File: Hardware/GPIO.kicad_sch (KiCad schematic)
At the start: 8 parts, among them J2 GPIO Breakout

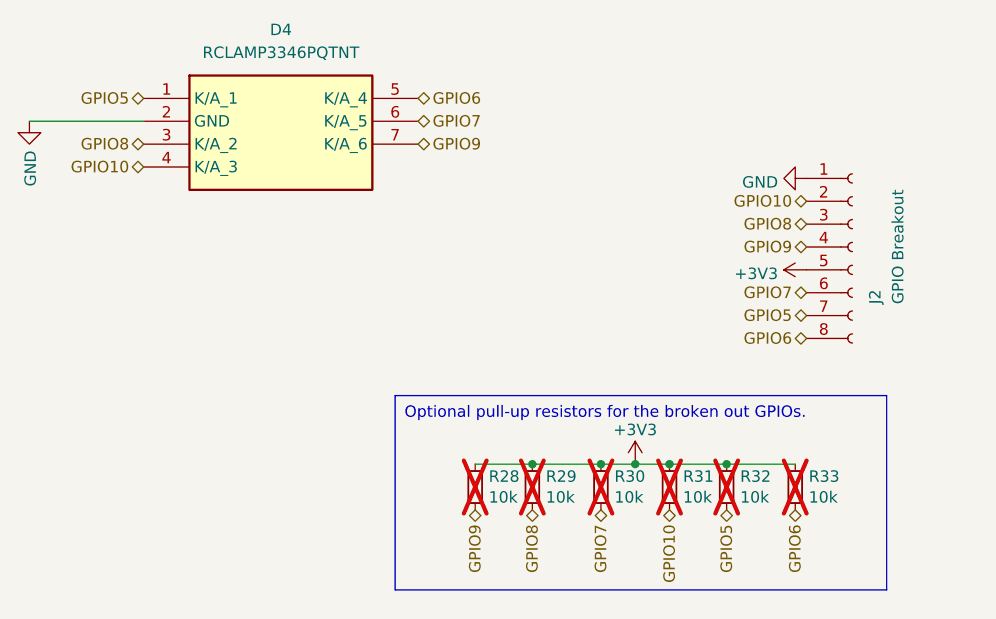
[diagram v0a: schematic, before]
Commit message: cleaned up schematic and bom
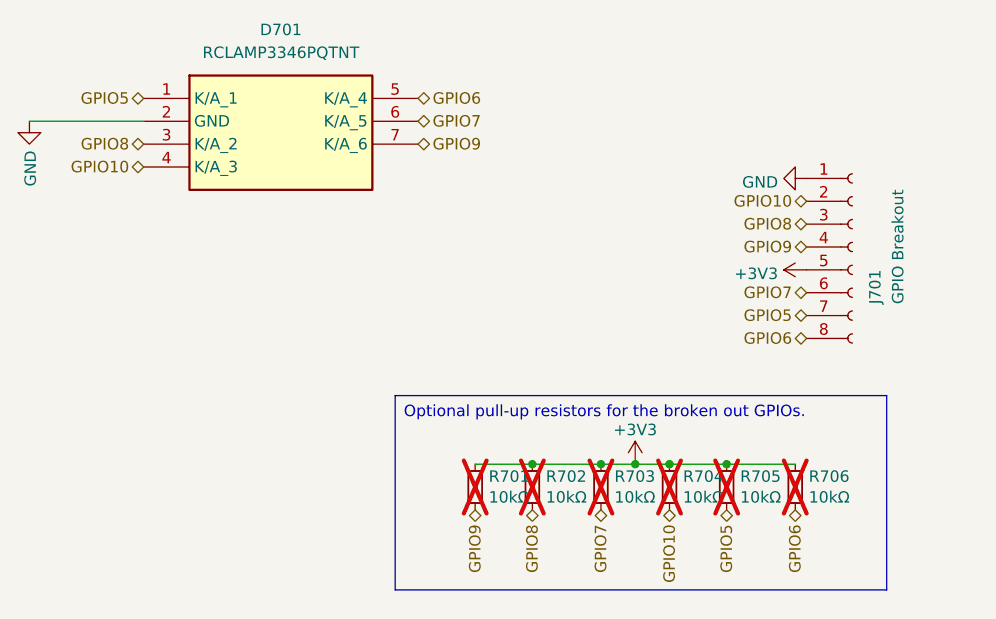
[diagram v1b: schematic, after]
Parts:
- R701: renamed from R28; value 10k -> 10kΩ
- R702: renamed from R29; value 10k -> 10kΩ
- R703: renamed from R30; value 10k -> 10kΩ
- R704: renamed from R31; value 10k -> 10kΩ
- R705: renamed from R32; value 10k -> 10kΩ
- R706: renamed from R33; value 10k -> 10kΩ
- renumbered D4 to D701, J2 to J701
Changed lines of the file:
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@@
 (kicad_sch
-	(version 20231120)
+	(version 20250114)
 	(generator "eeschema")
-	(generator_version "8.0")
+	(generator_version "9.0")
 	(paper "A4")
+	(text_box "Optional pull-up resistors for the broken out GPIOs."
+		(exclude_from_sim no)
+		(at 121.92 93.98 0)
+		(size 54.61 21.59)
+		(margins 0.9525 0.9525 0.9525 0.9525)
+		(stroke
+			(width 0)
+			(type default)
+		)
+		(fill
+			(type none)
+		)
+		(effects
+			(font
+				(size 1.27 1.27)
+			)
+			(justify left top)
+		)
+	)
 	(junction
 		(at 152.4 101.6)
@@
 		)
 	)
-	(text_box "Optional pull-up resistors for the broken out GPIOs."
-		(exclude_from_sim no)
-		(at 121.92 93.98 0)
-		(size 54.61 21.59)
-		(stroke
-			(width 0)
-			(type default)
-		)
-		(fill
-			(type none)
-		)
-		(effects
-			(font
-				(size 1.27 1.27)
-			)
-			(justify left top)
-		)
-	)
 	(hierarchical_label "GPIO6"
 		(shape bidirectional)
 		(at 124.46 60.96 0)
-		(fields_autoplaced yes)
 		(effects
 			(font
@@
 		(shape bidirectional)
 		(at 167.64 87.63 180)
-		(fields_autoplaced yes)
 		(effects
 			(font
@@
 		(shape bidirectional)
 		(at 167.64 85.09 180)
-		(fields_autoplaced yes)
 		(effects
 			(font
@@
 		(shape bidirectional)
 		(at 137.16 106.68 270)
-		(fields_autoplaced yes)
 		(effects
 			(font
@@
 		(shape bidirectional)
 		(at 144.78 106.68 270)
-		(fields_autoplaced yes)
 		(effects
 			(font
@@
 		(shape bidirectional)
 		(at 166.37 106.68 270)
-		(fields_autoplaced yes)
 		(effects
 			(font
@@
 		(shape bidirectional)
 		(at 124.46 66.04 0)
-		(fields_autoplaced yes)
 		(effects
 			(font
@@
 		(shape bidirectional)
 		(at 124.46 63.5 0)
-		(fields_autoplaced yes)
 		(effects
 			(font
@@
 		(shape bidirectional)
 		(at 167.64 82.55 180)
-		(fields_autoplaced yes)
 		(effects
 			(font
@@
 		(shape bidirectional)
 		(at 167.64 77.47 180)
-		(fields_autoplaced yes)
 		(effects
 			(font
@@
 		(shape bidirectional)
 		(at 130.81 106.68 270)
-		(fields_autoplaced yes)
 		(effects
 			(font
@@
 		(shape bidirectional)
 		(at 167.64 72.39 180)
-		(fields_autoplaced yes)
 		(effects
 			(font
@@
 		(shape bidirectional)
 		(at 93.98 66.04 180)
-		(fields_autoplaced yes)
 		(effects
 			(font
@@
 		(shape bidirectional)
 		(at 93.98 60.96 180)
-		(fields_autoplaced yes)
 		(effects
 			(font
@@
 		(shape bidirectional)
 		(at 93.98 68.58 180)
-		(fields_autoplaced yes)
 		(effects
 			(font
@@
 		(shape bidirectional)
 		(at 158.75 106.68 270)
-		(fields_autoplaced yes)
 		(effects
 			(font
@@
 		(shape bidirectional)
 		(at 152.4 106.68 270)
-		(fields_autoplaced yes)
 		(effects
 			(font
@@
 		(shape bidirectional)
 		(at 167.64 74.93 180)
-		(fields_autoplaced yes)
 		(effects
 			(font
@@
 		(on_board yes)
 		(dnp yes)
-		(property "Reference" "R28"
+		(property "Reference" "R701"
 			(at 132.3086 102.9716 0)
 			(effects
@@
 			)
 		)
-		(property "Value" "10k"
+		(property "Value" "10kΩ"
 			(at 132.3086 105.283 0)
 			(effects
@@
 			(project "Chad"
 				(path "/7db990e4-92e1-4f99-b4d2-435bbec1ba83/980abe29-0240-4f42-9b28-48e9ccaa9b3e"
-					(reference "R28")
+					(reference "R701")
 					(unit 1)
 				)
@@
 		(dnp no)
 		(fields_autoplaced yes)
-		(property "Reference" "#PWR026"
+		(property "Reference" "#PWR0702"
 			(at 148.59 105.41 0)
 			(effects
@@
 			(project "Chad"
 				(path "/7db990e4-92e1-4f99-b4d2-435bbec1ba83/980abe29-0240-4f42-9b28-48e9ccaa9b3e"
-					(reference "#PWR026")
+					(reference "#PWR0702")
 					(unit 1)
 				)
@@
 		(dnp no)
 		(fields_autoplaced yes)
-		(property "Reference" "D4"
+		(property "Reference" "D701"
 			(at 109.22 53.34 0)
 			(effects
@@
 			(project "Chad"
 				(path "/7db990e4-92e1-4f99-b4d2-435bbec1ba83/980abe29-0240-4f42-9b28-48e9ccaa9b3e"
-					(reference "D4")
+					(reference "D701")
 					(unit 1)
 				)
@@
 		(on_board yes)
 		(dnp no)
-		(property "Reference" "#PWR09"
+		(property "Reference" "#PWR0701"
 			(at 81.28 69.85 0)
 			(effects
@@
 			(project "Chad"
 				(path "/7db990e4-92e1-4f99-b4d2-435bbec1ba83/980abe29-0240-4f42-9b28-48e9ccaa9b3e"
-					(reference "#PWR09")
+					(reference "#PWR0701")
 					(unit 1)
 				)
@@
 		(on_board yes)
 		(dnp no)
-		(property "Reference" "J2"
+		(property "Reference" "J701"
 			(at 175.26 83.82 90)
 			(effects
@@
 			(project "Chad"
 				(path "/7db990e4-92e1-4f99-b4d2-435bbec1ba83/980abe29-0240-4f42-9b28-48e9ccaa9b3e"
-					(reference "J2")
+					(reference "J701")
 					(unit 1)
 				)
@@
 		(dnp no)
 		(fields_autoplaced yes)
-		(property "Reference" "#PWR027"
+		(property "Reference" "#PWR0703"
 			(at 161.29 69.85 0)
 			(effects
@@
 			(project "Chad"
 				(path "/7db990e4-92e1-4f99-b4d2-435bbec1ba83/980abe29-0240-4f42-9b28-48e9ccaa9b3e"
-					(reference "#PWR027")
+					(reference "#PWR0703")
 					(unit 1)
 				)
@@
 		(on_board yes)
 		(dnp yes)
-		(property "Reference" "R29"
+		(property "Reference" "R702"
 			(at 138.6586 102.9716 0)
 			(effects
@@
 			)
 		)
-		(property "Value" "10k"
+		(property "Value" "10kΩ"
 			(at 138.6586 105.283 0)
 			(effects
@@
 			(project "Chad"
 				(path "/7db990e4-92e1-4f99-b4d2-435bbec1ba83/980abe29-0240-4f42-9b28-48e9ccaa9b3e"
-					(reference "R29")
+					(reference "R702")
 					(unit 1)
 				)
@@
 		(on_board yes)
 		(dnp yes)
-		(property "Reference" "R33"
+		(property "Reference" "R706"
 			(at 167.8686 102.9716 0)
 			(effects
@@
 			)
 		)
-		(property "Value" "10k"
+		(property "Value" "10kΩ"
 			(at 167.8686 105.283 0)
 			(effects
@@
 			(project "Chad"
 				(path "/7db990e4-92e1-4f99-b4d2-435bbec1ba83/980abe29-0240-4f42-9b28-48e9ccaa9b3e"
-					(reference "R33")
+					(reference "R706")
 					(unit 1)
 				)
@@
 		(on_board yes)
 		(dnp yes)
-		(property "Reference" "R32"
+		(property "Reference" "R705"
 			(at 160.2486 102.9716 0)
 			(effects
@@
 			)
 		)
-		(property "Value" "10k"
+		(property "Value" "10kΩ"
 			(at 160.2486 105.283 0)
 			(effects
@@
 			(project "Chad"
 				(path "/7db990e4-92e1-4f99-b4d2-435bbec1ba83/980abe29-0240-4f42-9b28-48e9ccaa9b3e"
-					(reference "R32")
+					(reference "R705")
 					(unit 1)
 				)
@@
 		(dnp no)
 		(fields_autoplaced yes)
-		(property "Reference" "#PWR079"
+		(property "Reference" "#PWR0704"
 			(at 171.45 80.01 0)
 			(effects
@@
 			(project "Chad"
 				(path "/7db990e4-92e1-4f99-b4d2-435bbec1ba83/980abe29-0240-4f42-9b28-48e9ccaa9b3e"
-					(reference "#PWR079")
+					(reference "#PWR0704")
 					(unit 1)
 				)
@@
 		(on_board yes)
 		(dnp yes)
-		(property "Reference" "R30"
+		(property "Reference" "R703"
 			(at 146.2786 102.9716 0)
 			(effects
@@
 			)
 		)
-		(property "Value" "10k"
+		(property "Value" "10kΩ"
 			(at 146.2786 105.283 0)
 			(effects
@@
 			(project "Chad"
 				(path "/7db990e4-92e1-4f99-b4d2-435bbec1ba83/980abe29-0240-4f42-9b28-48e9ccaa9b3e"
-					(reference "R30")
+					(reference "R703")
 					(unit 1)
 				)
@@
 		(on_board yes)
 		(dnp yes)
-		(property "Reference" "R31"
+		(property "Reference" "R704"
 			(at 153.8986 102.9716 0)
 			(effects
@@
 			)
 		)
-		(property "Value" "10k"
+		(property "Value" "10kΩ"
 			(at 153.8986 105.283 0)
 			(effects
@@
 			(project "Chad"
 				(path "/7db990e4-92e1-4f99-b4d2-435bbec1ba83/980abe29-0240-4f42-9b28-48e9ccaa9b3e"
-					(reference "R31")
+					(reference "R704")
 					(unit 1)
 				)
